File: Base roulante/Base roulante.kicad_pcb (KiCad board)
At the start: 2 copper layers, 76.2 x 85.1 mm, 15 parts, among them J1 RJ_can, J2 RJ_can, J5 connector_power, U1 Blue Pill, U2 MCP2551-I-SN

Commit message: Update base roulante
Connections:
- U1 pad 1: unconnected-(U1-Pad1) -> DIR_G
- U1 pad 2: unconnected-(U1-Pad2) -> DIR_D
- U1 pad 25: A_D -> unconnected-(U1-Pad25)
- U1 pad 26: B_D -> unconnected-(U1-Pad26)
- U1 pad 31: DIR_D -> A_D
- U1 pad 32: DIR_G -> B_D
- U1 pad 33: PWM_D -> unconnected-(U1-Pad33)
- U1 pad 34: PWM_G -> unconnected-(U1-Pad34)
- U1 pad 5: unconnected-(U1-Pad5) -> PWM_G
- U1 pad 6: unconnected-(U1-Pad6) -> PWM_D
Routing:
- net PWM_G: track 23.5 -> 63.0 mm
- net PWM_D: track 61.3 -> 30.9 mm
- net DIR_G: track 36.3 -> 61.1 mm
- net DIR_D: track 61.1 -> 45.1 mm, vias 1 -> 0
- net A_D: track 61.2 -> 73.2 mm, vias 0 -> 1
- net +5V: track 205.6 -> 210.1 mm
- net +12V: track 96.4 -> 99.0 mm
- net B_D: track 69.3 -> 70.5 mm, vias 0 -> 1
- net CANH: track 34.0 -> 34.6 mm

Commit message: Update base roulante
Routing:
- net +5V: track 210.1 -> 212.8 mm
- net PWM_D: track 30.9 -> 32.0 mm
- net CAN_RX: track 56.8 -> 57.6 mm
- net +12V: track 99.0 -> 98.3 mm

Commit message: Commande
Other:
- board text added: "AAB Louis Chauvet"
- board text added: "JLCJLCJLCJLC"

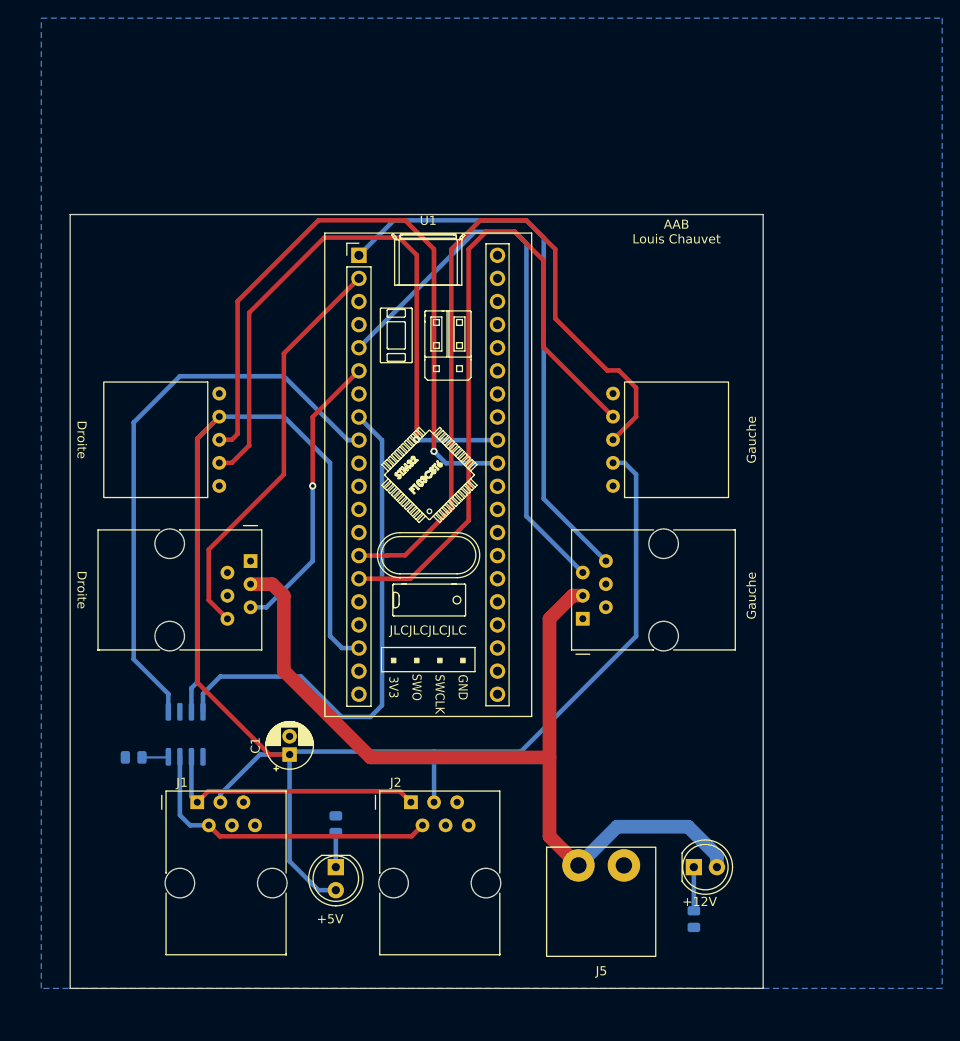
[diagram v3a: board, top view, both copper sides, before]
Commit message: Update card to cut board near to the connector
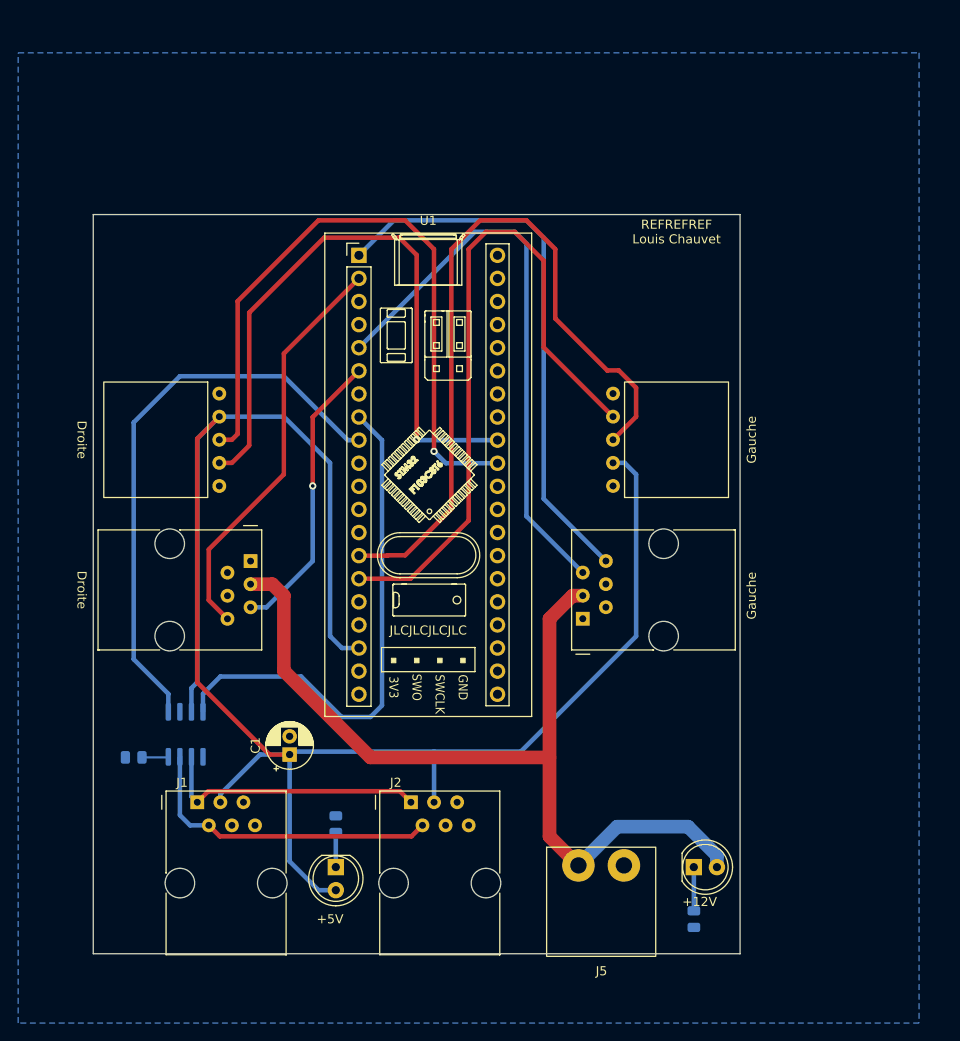
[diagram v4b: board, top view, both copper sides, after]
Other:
- board size 76.2 x 85.1 mm -> 71.1 x 81.3 mm
- board text added: "REFREFREF Louis Chauvet"
- board text removed: "AAB Louis Chauvet"

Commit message: Add Base roulante updated
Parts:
- added C2: 470u, Capacitor_THT:CP_Radial_D5.0mm_P2.00mm, F.Cu at (152.7, 103.5)
- added DPANIC1: LED Rouge, LED_SMD:LED_0805_2012Metric, F.Cu at (105.7, 108.0)
- added R4: 330, Resistor_SMD:R_0805_2012Metric, B.Cu at (105.7, 108.0)
- C1: value C_Polarized -> 47u
- D+12V1: value LED -> LED bleu; footprint LED_THT:LED_D5.0mm -> LED_SMD:LED_0805_2012Metric
- D+5V1: value LED -> LED Verte; footprint LED_THT:LED_D5.0mm -> LED_SMD:LED_0805_2012Metric
- R1: value R -> 330
- R2: value R -> 10k
- R3: value R -> 1k
- moved D+12V1 62.7 mm to (105.7, 115.6)
- moved R3 62.5 mm to (105.8, 115.6), turned to 0 degrees
- moved R1 23.7 mm to (105.8, 111.8), turned to 0 degrees
- moved D+5V1 23.2 mm to (105.7, 111.8), turned to 0 degrees
- moved J1 3.81 mm to (117.5, 104.0)
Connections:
- U1 pad 16: unconnected-(U1-Pad16) -> PANIC
- U1 pad 20: unconnected-(U1-Pad20) -> +3.3V
- U1 pad 38: unconnected-(U1-Pad38) -> +3.3V
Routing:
- net +3.3V: track 0.00 -> 115.7 mm, vias 0 -> 1
- net PANIC: track 0.00 -> 60.3 mm, vias 0 -> 3
- net +12V: track 98.3 -> 131.7 mm
- net +5V: track 212.8 -> 216.0 mm
- net CANL: track 29.8 -> 27.5 mm
- net Net-(D+12V1-Pad1): track 4.80 -> 2.65 mm, vias 0 -> 1
- net Net-(D+5V1-Pad1): track 3.81 -> 2.65 mm, vias 0 -> 1
- added copper zone on F.Cu, net GND
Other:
- board text added: "PANIC"
